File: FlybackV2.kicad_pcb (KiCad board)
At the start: 2 copper layers, 183.1 x 109.3 mm, 148 parts, among them J1 Power, J10 ads1256, J11 Coils, J2 Conn_01x02, J3 Conn_01x03, T2 0399-T208, U1 LT8304, U10 LT1634BIS8-2.5, U11 MAX4239, U2 TEA 1-0505, U4 7.68MHz, U5 MAX4239, U6 MAX4239, U7 MAX4239, U8 ADS1256IDBR, U9 MAX4239

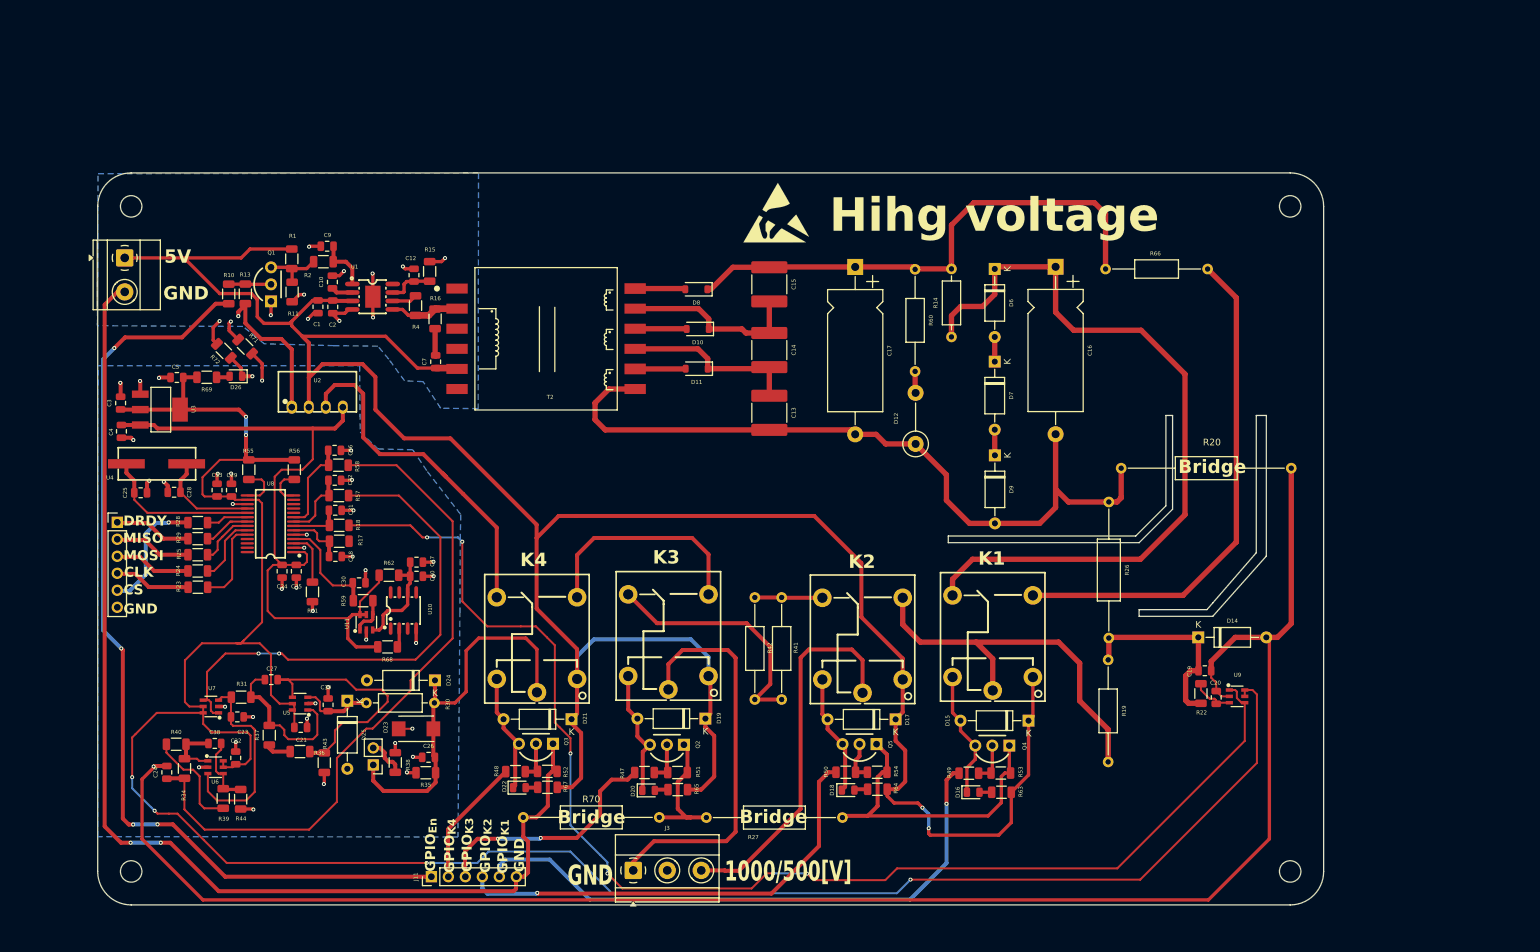
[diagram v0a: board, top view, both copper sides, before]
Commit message: v2 now with pnp transistor
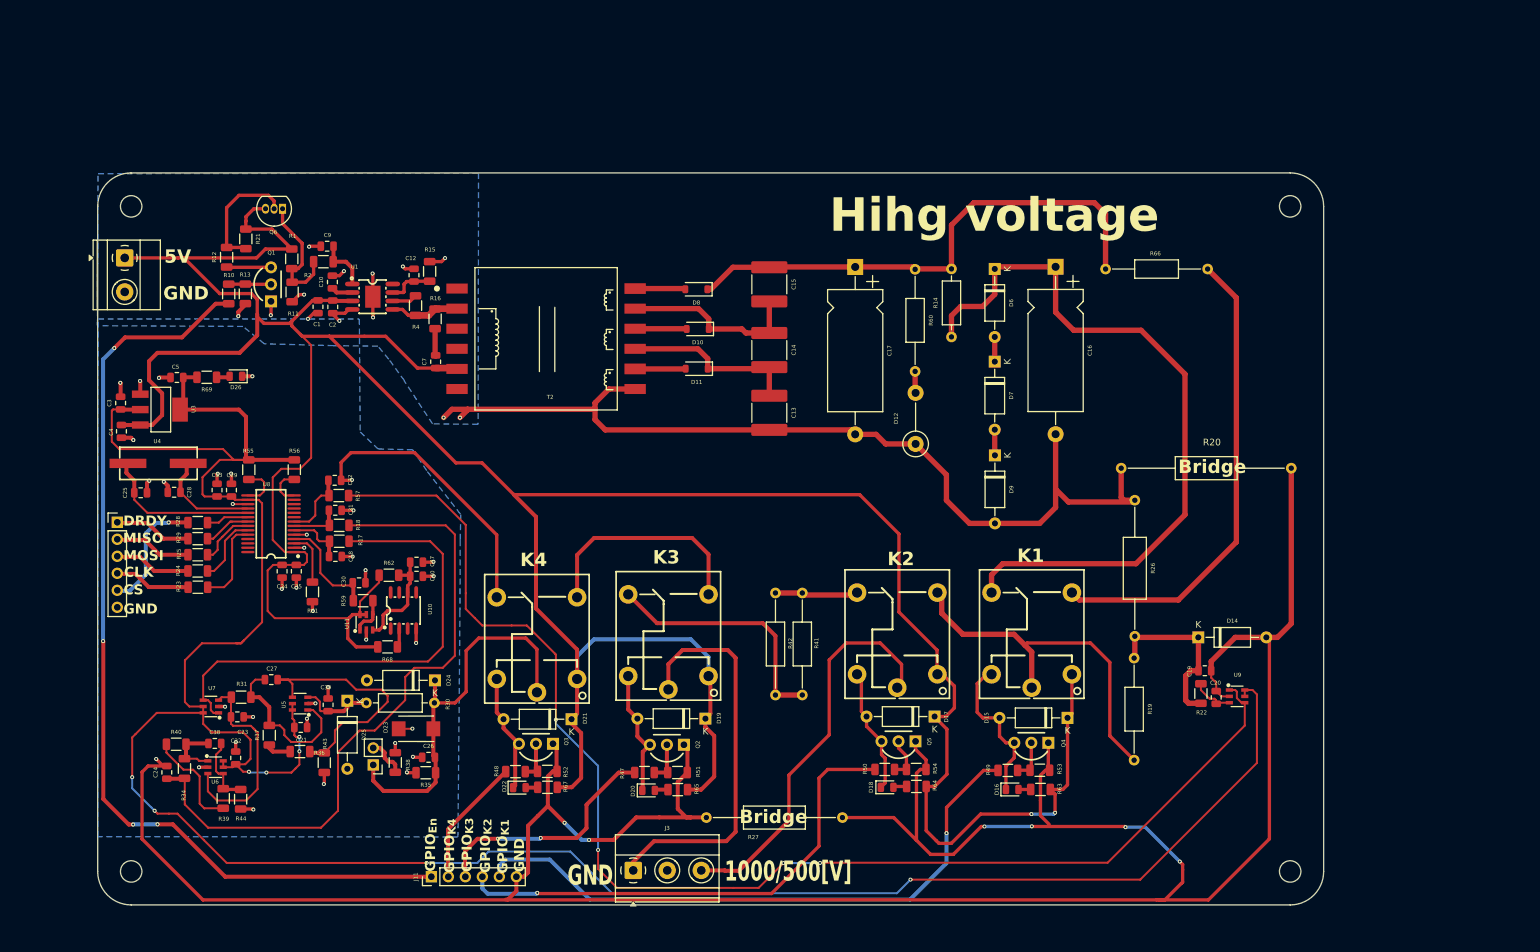
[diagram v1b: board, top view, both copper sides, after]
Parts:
- removed C36: 100nF, Capacitor_SMD:C_0805_2012Metric
- removed R58: 1K, Resistor_SMD:R_1206_3216Metric
- removed R70: 0, Resistor_THT:R_Axial_DIN0309_L9.0mm_D3.2mm_P20.32mm_Horizontal
- removed R71, R72: 0, Resistor_SMD:R_1206_3216Metric
- removed REF**: ESD-Logo_6.6x6mm_SilkScreen, Symbol:ESD-Logo_6.6x6mm_SilkScreen
- removed U2: TEA 1-0505, JuanDavid_Library:SIP-4_L11.7-W6.0-P2.54_B0505S-1W
- added Q6: 2N3906, Package_TO_SOT_THT:TO-92_Inline, F.Cu at (82.8, 47.8)
- added R12: 560, Resistor_SMD:R_1206_3216Metric, F.Cu at (74.4, 55.0)
- added R21: 1K, Resistor_SMD:R_1206_3216Metric, F.Cu at (77.3, 52.3)
- moved D15 5.84 mm to (200.0, 123.8)
- moved D16 5.84 mm to (191.8, 134.5)
- moved D17 5.84 mm to (180.2, 123.6)
- moved D18 5.84 mm to (173.1, 134.2)
- moved Q4 5.84 mm to (194.6, 127.5)
- moved Q5 5.84 mm to (174.8, 127.3)
- moved R49 5.84 mm to (191.1, 131.7)
- moved R50 5.84 mm to (172.7, 131.5)
- moved R53 5.84 mm to (195.9, 131.6)
- moved R63 5.84 mm to (196.0, 134.5)
- moved R64 5.84 mm to (177.5, 134.1)
- moved R32 5.84 mm to (194.7, 112.2)
- moved R54 5.84 mm to (177.4, 131.5)
- moved R33 5.24 mm to (174.6, 112.2)
- moved R19 3.89 mm to (210.0, 114.9)
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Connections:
- C13 pad 2: GND2 -> GND
- C16 pad 2: GND2 -> GND
- C17 pad 2: GND2 -> GND
- C18 pad 2: GND2 -> GND
- C19 pad 1: GND2 -> GND
- C20 pad 1: GND2 -> GND
- C21 pad 2: GND2 -> GND
- C22 pad 2: GND2 -> GND
- C23 pad 2: GND2 -> GND
- C24 pad 1: /ADC3 -> /ADC1
- C24 pad 2: GND2 -> GND
- C25 pad 2: GND2 -> GND
- C26 pad 1: GND2 -> GND
- C28 pad 1: GND2 -> GND
- C29 pad 2: GND2 -> GND
- C3 pad 2: GND2 -> GND
- C30 pad 2: GND2 -> GND
- C31 pad 2: GND2 -> GND
- C32 pad 2: GND2 -> GND
- C33 pad 2: GND2 -> GND
- C34 pad 1: 5_{iso}V -> +5V
- C34 pad 2: GND2 -> GND
- C35 pad 1: 5_{iso}V -> +5V
- C35 pad 2: GND2 -> GND
- C37 pad 2: GND2 -> GND
- C39 pad 1: GND2 -> GND
- C4 pad 1: 5_{iso}V -> +5V
- C4 pad 2: GND2 -> GND
- C40 pad 2: GND2 -> GND
- C5 pad 2: GND2 -> GND
- D12 pad 1: GND2 -> GND
- D14 pad 2: GND2 -> GND
- D23 pad 1: GND2 -> GND
- D24 pad 2: GND2 -> GND
- D25 pad 2: GND2 -> GND
- D26 pad 1: GND2 -> GND
- D9 pad 2: GND2 -> GND
- J10 pad 6: GND2 -> GND
- R1 pad 2: Net-(Q1-Pad3) -> Net-(Q6-E)
- R11 pad 1: Net-(Q1-Pad3) -> Net-(Q6-E)
- R2 pad 2: Net-(Q1-Pad3) -> Net-(Q6-E)
- R20 pad 1: GND2 -> GND
- R20 pad 2: GND2 -> GND
- R26 pad 1: GND2 -> GND
- R34 pad 2: /ADC3 -> /ADC1
- R35 pad 2: GND2 -> GND
- R38 pad 2: GND2 -> GND
- R43 pad 2: GND2 -> GND
- R44 pad 2: GND2 -> GND
- R46 pad 3: GND2 -> GND
- R61 pad 1: GND2 -> GND
- R62 pad 1: 5_{iso}V -> +5V
- R68 pad 1: 5_{iso}V -> +5V
- T2 pad 7: GND2 -> GND
- U10 pad 4: GND2 -> GND
- U11 pad 2: GND2 -> GND
- U11 pad 5: 5_{iso}V -> +5V
- U11 pad 6: 5_{iso}V -> +5V
- U3 pad 1: GND2 -> GND
- U3 pad 3: 5_{iso}V -> +5V
- U5 pad 2: GND2 -> GND
- U6 pad 2: GND2 -> GND
- U7 pad 1: /ADC2 -> /ADC0
- U7 pad 2: GND2 -> GND
- U7 pad 4: /ADC2 -> /ADC0
- U8 pad 1: 5_{iso}V -> +5V
- U8 pad 17: GND2 -> GND
- U8 pad 2: GND2 -> GND
- U8 pad 5: GND2 -> GND
- U8 pad 9: Net-(U8-AIN3) -> unconnected-(U8-AIN3-Pad9)
- U9 pad 1: /ADC1 -> /ADC2
- U9 pad 2: GND2 -> GND
- U9 pad 4: /ADC1 -> /ADC2
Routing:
- net GND2: track 501.3 -> 0.00 mm, vias 39 -> 0
- net GND: track 297.5 -> 701.0 mm, vias 15 -> 56
- net +5V: track 378.0 -> 517.0 mm
- net /ADC2: track 76.8 -> 197.6 mm, vias 2 -> 4
- net 5_{iso}V: track 107.1 -> 0.00 mm
- net /ADC3: track 101.7 -> 0.00 mm
- net /ADC1: track 196.1 -> 100.6 mm, vias 6 -> 0
- net /ADC0: track 0.00 -> 73.6 mm
- net +3.3_{iso}V: track 357.7 -> 380.2 mm, vias 6 -> 8
- net Net-(Q6-E): track 0.00 -> 19.0 mm
- net Net-(Q6-B): track 0.00 -> 18.2 mm
- net Net-(U8-AIN3): track 13.8 -> 0.00 mm
- net /GPIO_{K2}: track 68.1 -> 74.4 mm
- net 500V: track 116.2 -> 110.1 mm
- net Net-(R32-Pad2): track 76.2 -> 71.1 mm
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- removed copper zone on B.Cu, net GND2
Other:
- outline, holes or cut-outs redrawn

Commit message: finish v2 version
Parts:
- removed R20: 0, Resistor_THT:R_Axial_DIN0309_L9.0mm_D3.2mm_P25.40mm_Horizontal
- removed R27: 0, Resistor_THT:R_Axial_DIN0309_L9.0mm_D3.2mm_P20.32mm_Horizontal
- removed R30: 100, Resistor_THT:R_Axial_DIN0207_L6.3mm_D2.5mm_P10.16mm_Horizontal
- added C36: 10u, Capacitor_SMD:C_0805_2012Metric, F.Cu at (69.1, 124.3)
- added C41: 10u, Capacitor_SMD:C_0805_2012Metric, F.Cu at (91.3, 108.7)
- added C42: 10u, Capacitor_SMD:C_0805_2012Metric, F.Cu at (227.4, 117.3)
- added R58: 100, Resistor_SMD:R_1206_3216Metric, F.Cu at (100.9, 121.4)
- D12: footprint Resistor_THT:R_Axial_DIN0411_L9.9mm_D3.6mm_P7.62mm_Vertical -> LED_SMD:LED_0805_2012Metric
- moved R41 9.73 mm to (159.4, 110.7)
- moved R42 9.73 mm to (155.4, 110.7)
- moved D12 5.65 mm to (177.2, 77.2)
- moved H3 4.91 mm to (59.3, 151.6)
- moved H2 4.87 mm to (234.0, 151.6)
- moved Q6 2.64 mm to (80.2, 47.7), turned to 0 degrees
- moved D26 1.87 mm to (76.5, 71.0)
- moved C3 1.87 mm to (59.2, 75.0)
- moved C5 1.87 mm to (67.6, 71.2)
- moved C4 1.87 mm to (59.4, 79.3)
- moved R69 1.87 mm to (72.1, 71.2)
- moved U3 1.87 mm to (65.1, 76.0)
- moved H4 0.94 mm to (59.3, 47.3)
- moved H1 0.69 mm to (234.0, 47.3)
- moved R22 0.35 mm to (219.6, 120.1)
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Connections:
- Q6 pad 1: Net-(Q6-E) -> +5V
- Q6 pad 3: +5V -> Net-(Q6-C)
- R1 pad 2: Net-(Q6-E) -> Net-(Q6-C)
- R11 pad 1: Net-(Q6-E) -> Net-(Q6-C)
- R2 pad 2: Net-(Q6-E) -> Net-(Q6-C)
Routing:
- net GND: track 701.0 -> 666.6 mm, vias 56 -> 60
- net Net-(Q6-E): track 19.0 -> 0.00 mm
- net Net-(Q6-C): track 0.00 -> 18.4 mm
- net Net-(R41-Pad1): track 37.4 -> 27.2 mm
- net Net-(D25-K): track 11.8 -> 20.9 mm
- net Net-(R33-Pad3): track 12.5 -> 19.8 mm
- net /ADC2: track 197.6 -> 204.5 mm, vias 4 -> 2
- net Net-(U5-IN-): track 38.7 -> 42.6 mm
- net /GPIO_{K2}: track 74.4 -> 78.0 mm
- net +5V: track 517.0 -> 520.5 mm
- net /In_{pos}: track 58.4 -> 61.6 mm
- net /GPIO_{K1}: track 91.9 -> 94.9 mm
- net Net-(R19-Pad2): track 54.6 -> 57.5 mm
- net /GPIO_{K3}: track 36.1 -> 34.0 mm
- net +3.3_{iso}V: track 380.2 -> 378.3 mm
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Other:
- board size 183.1 x 109.3 mm -> 184.7 x 114.2 mm
- board text added: "F2"
- board text removed: "Bridge"

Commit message: update: init the track of the pcb
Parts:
- removed C18, C31, C32: 100nF, Capacitor_SMD:C_0805_2012Metric
- removed C21, C22, C23, C24, C29, C30, C34, C36, C37, C41: 10u, Capacitor_SMD:C_0805_2012Metric
- removed C25, C28: 20pF, Capacitor_SMD:C_0805_2012Metric
- removed C26, C27, C38, C39: 1u, Capacitor_SMD:C_0805_2012Metric
- removed C33, C35, C40: 0.1u, Capacitor_SMD:C_0805_2012Metric
- removed D19, D21: D_Small_Filled, Diode_THT:D_A-405_P10.16mm_Horizontal
- removed D20, D22: LED, LED_SMD:LED_0805_2012Metric
- removed D23: SMBJ5.0CA, JuanDavid_Library:SMB_L4.6-W3.6-LS5.3-BI
- removed D24, D25: D_Zener_Small_Filled, Diode_THT:D_A-405_P10.16mm_Horizontal
- removed J10: ads1256, Connector_PinHeader_2.54mm:PinHeader_1x06_P2.54mm_Vertical
- removed J11: Coils, Connector_PinHeader_2.54mm:PinHeader_1x06_P2.54mm_Vertical
- removed Q2, Q3: ~, JuanDavid_Library:TO-92-3_L4.9-W3.7-P2.54-L
- removed R17, R18, R43, R44, R51, R52, R57, R65: 1K, Resistor_SMD:R_1206_3216Metric
- removed R23, R24, R25, R28, R29, R31, R34, R55, R56, R58, R59: 100, Resistor_SMD:R_1206_3216Metric
- removed R35: 10K, Resistor_SMD:R_1206_3216Metric
- removed R36, R39: 2.2K, Resistor_SMD:R_1206_3216Metric
- removed R37, R40: 6.8K, Resistor_SMD:R_1206_3216Metric
- removed R38: 10, Resistor_SMD:R_1206_3216Metric
- removed R45, R46: ~, JuanDavid_Library:RELAY-TH_SRD-XXVDC-XL-C
- removed R47, R48: 560, Resistor_SMD:R_1206_3216Metric
- removed R61, R68: 0, Resistor_SMD:R_1206_3216Metric
- removed R62: 4, Resistor_SMD:R_1206_3216Metric
- removed U10: LT1634BIS8-2.5, JuanDavid_Library:SO-8_L4.9-W3.9-P1.27-LS5.9-BL
- removed U11, U5, U6, U7: MAX4239, JuanDavid_Library:SOT-23-6_L2.9-W1.6-P0.95-LS2.9-BL
- removed U4: 7.68MHz, JuanDavid_Library:CRYSTAL-SMD_L11.4-W4.7-LS12.4
- removed U8: ADS1256IDBR, JuanDavid_Library:SSOP-28_L10.2-W5.3-P0.65-LS7.8-BL
- added J4: Coils, Connector_PinHeader_2.54mm:PinHeader_1x05_P2.54mm_Vertical, F.Cu at (67.0, 74.0)
- J2: value Conn_01x02 -> Divisor; footprint Connector_PinHeader_2.54mm:PinHeader_1x02_P2.54mm_Vertical -> TerminalBlock_Phoenix:TerminalBlock_Phoenix_MKDS-1,5-2-5.08_1x02_P5.08mm_Horizontal
- R26: value 47M -> 100K
- R67: value 1K -> 2M; footprint Resistor_SMD:R_1206_3216Metric -> Resistor_THT:R_Axial_DIN0207_L6.3mm_D2.5mm_P15.24mm_Horizontal
- moved J3 142.6 mm to (263.2, 83.7), turned to 90 degrees
- moved R67 118.1 mm to (207.3, 52.1), turned to 180 degrees
- moved J2 106.6 mm to (201.0, 110.7), turned to 0 degrees
- moved R63 89.8 mm to (251.8, 64.1), turned to 90 degrees
- moved D16 89.4 mm to (251.8, 68.3), turned to 90 degrees
- moved D18 88.8 mm to (250.9, 91.4), turned to 90 degrees
- moved R64 87.1 mm to (250.8, 87.0), turned to 90 degrees
- moved R53 85.8 mm to (248.9, 64.2), turned to 90 degrees
- moved R50 85.4 mm to (248.3, 91.7), turned to -90 degrees
- moved R49 85.3 mm to (249.0, 69.0), turned to -90 degrees
- moved R54 83.6 mm to (248.3, 87.0), turned to 90 degrees
- moved R42 80.4 mm to (235.8, 109.0), turned to 180 degrees
- moved Q4 79.8 mm to (244.8, 65.5), turned to -90 degrees
- moved Q5 78.8 mm to (244.1, 89.7), turned to -90 degrees
- moved R41 76.6 mm to (235.8, 105.0), turned to 180 degrees
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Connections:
- J2 pad 1: /In_{pos} -> Net-(J2-Pin_1)
- J2 pad 2: Net-(J2-Pin_2) -> GND
- R32 pad 3: 500V -> Net-(R32-Pad3)
- R41 pad 1: Net-(R41-Pad1) -> Net-(J3-Pin_1)
- R42 pad 1: Net-(R41-Pad1) -> Net-(J3-Pin_1)
- R67 pad 1: Net-(D22-A) -> Net-(R32-Pad3)
- R67 pad 2: +5V -> 500V
- U9 pad 1: /ADC2 -> Net-(J2-Pin_1)
- U9 pad 4: /ADC2 -> Net-(J2-Pin_1)
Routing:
- net GND: track 666.6 -> 139.5 mm, vias 60 -> 0
- net +3.3_{iso}V: track 378.3 -> 24.7 mm, vias 8 -> 0
- net /ADC2: track 204.5 -> 0.00 mm, vias 2 -> 0
- net /GPIO_{EN}: track 141.7 -> 24.9 mm, vias 4 -> 0
- net /ADC1: track 101.2 -> 0.00 mm
- net /GPIO_{K1}: track 94.9 -> 0.00 mm, vias 1 -> 0
- net 500V: track 110.4 -> 31.0 mm
- net /GPIO_{K2}: track 78.0 -> 0.00 mm, vias 1 -> 0
- net /ADC0: track 73.6 -> 0.00 mm
- net /In_{pos}: track 61.6 -> 0.00 mm
- net Net-(R32-Pad2): track 71.1 -> 25.7 mm
- net Net-(U5-IN-): track 42.6 -> 0.00 mm
- net /GPIO_{K3}: track 34.0 -> 0.00 mm, vias 2 -> 0
- net Net-(R45-Pad2): track 34.0 -> 0.00 mm
- net +5V: track 520.5 -> 551.1 mm, vias 2 -> 0
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- removed copper zone on B.Cu, net GND
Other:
- board size 184.7 x 114.2 mm -> 203.9 x 76.9 mm
- board text added: "GPIO_{EN}"
- board text removed: "1000/500[V]"
- board text removed: "CLK"
- board text removed: "CS"
- board text removed: "DRDY"
- board text removed: "F2"
- board text removed: "GPIO_{En}"
- board text removed: "GPIO_{K3}"
- board text removed: "GPIO_{K4}"
- board text removed: "K3"
- board text removed: "K4"
- board text removed: "MISO"
- board text removed: "MOSI"

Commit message: finish the route, in revision
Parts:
- added REF**: Symbol_HighVoltage_Triangle_6x6mm_Copper, Symbol:Symbol_HighVoltage_Triangle_6x6mm_Copper, F.Cu at (115.3, 66.8)
- moved H1 25.6 mm to (243.2, 62.0)
- moved D10 25.6 mm to (127.2, 84.3)
- moved C10 25.6 mm to (71.8, 78.5)
- moved D17 25.6 mm to (222.8, 102.9)
- moved H2 25.6 mm to (243.2, 128.5)
- moved H3 25.6 mm to (50.1, 128.4)
- moved H4 25.6 mm to (50.1, 61.5)
- moved Q6 25.6 mm to (62.6, 66.3)
- moved R10 25.6 mm to (56.8, 79.1)
- moved R12 25.6 mm to (56.8, 73.6)
- moved R21 25.6 mm to (59.6, 70.7)
- moved C9 25.6 mm to (71.8, 73.8)
- moved D11 25.6 mm to (127.0, 90.2)
- moved D26 25.6 mm to (75.1, 98.0)
- moved J2 25.6 mm to (183.4, 129.3)
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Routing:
- net GND: track 139.5 -> 585.8 mm, vias 0 -> 27
- net /GPIO_{K1}: track 0.00 -> 265.7 mm, vias 0 -> 2
- net /GPIO_{K2}: track 0.00 -> 211.3 mm, vias 0 -> 2
- net +3.3_{iso}V: track 24.7 -> 159.0 mm, vias 0 -> 4
- net Net-(C7-Pad2): track 0.00 -> 4.02 mm
- net Net-(J3-Pin_1): track 47.2 -> 50.4 mm
- net Net-(J3-Pin_3): track 49.3 -> 51.4 mm
- net Net-(R32-Pad3): track 28.5 -> 30.7 mm
- net +5V: track 551.1 -> 552.6 mm
- net Net-(R19-Pad2): track 50.6 -> 49.4 mm
- added copper zone on B.Cu, net GND
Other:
- board size 203.9 x 76.9 mm -> 205.7 x 77.7 mm
- board text added: "1000/500V"
- board text added: "DIV"
- board text added: "Dischard"
- board text added: "NC"
